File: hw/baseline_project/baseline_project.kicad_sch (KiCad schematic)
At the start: 17 parts, among them J101 EXT_3V3, Q101 IRLD024PBF, SW101 UP, SW102 DOWN, SW103 LEFT, SW104 RIGHT, SW105 MODE, U101 EK-TM4C123GXL, U102 ESP8266-01/ESP-01, U103 Adafruit ST7735R

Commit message: schematic
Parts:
- removed D101: 1V0, Diode_THT:D_5W_P12.70mm_Horizontal, symbol Device:D_Small
- removed LS101: Speaker, Connector_PinHeader_2.54mm:PinHeader_1x02_P2.54mm_Vertical, symbol Device:Speaker
- removed Q101: IRLD024PBF, footprints:vishay_IRLD024PBF, symbol Simulation_SPICE:NMOS
- added C1: 1uF, symbol Device:C
- added C2: 0.1uF, symbol Device:C
- added C3, C4, C5: 4.7uF, symbol Device:C
- added IC1: LM4041CILPR, ECE445L:ti_LM4041CILPR, symbol ti_LM4041CILPR:LM4041CILPR
- added J1: AudioJack, ECE445L:Jack_3.5mm_CUI_SJ1-3523N_Horizontal, symbol ECE445L:HeadphoneJack
- added JP1: Jumper_3_Open, ECE445L:PinHeader_1x03_P2.54mm_Vertical, symbol ECE445L:Jumper_3_Open
- added R1: 20k, symbol Device:R
- added R10, R2, R5, R6, R7, R8, R9: 10k, symbol Device:R
- added R11: 10k, ECE445L:Potentiometer, symbol ECE445L:Potentiometer
- added R3: 2k, symbol Device:R
- added R4: 47k, symbol Device:R
- added TP1, TP2, TP3, TP4, TP5, TP6: TP, ECE445L:Testpoint_1x02_P2.54mm, symbol ECE445L:Testpoint
- added U1: TLV5616CP, symbol ti_TLV5616CP:TLV5616CP
- added U2: MCP34119P, Package_DIP:DIP-8_W7.62mm_LongPads, symbol motorola_MCP34119P:MCP34119P
- added U3: LM2937xMP, Package_TO_SOT_SMD:SOT-223-3_TabPin2, symbol Regulator_Linear:LM2937xMP
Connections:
- net +3V3: now also SW101.1, SW102.1, SW103.1, SW104.1, SW105.1, JP1.1 (A), R11.1, TP5.1 (A), TP5.2 (B)
- net +5V: now also C4.1, TP4.1 (A), TP4.2 (B), U3.1 (VI)
- net GND: now also C1.2, C3.2, C4.2, C5.2, IC1.3, R10.2, R11.3, R5.2, R6.2, R7.2, R8.2, R9.2, TP6.1 (A), TP6.2 (B), U1.3 (*CS), U1.5 (AGND), U2.1 (CD), U2.7 (GND), U3.2 (GND); no longer SW101.1, SW102.1, SW103.1, SW104.1, SW105.1
- net SW_DOWN: now also R7.1
- net SW_LEFT: now also R8.1
- net SW_MODE: now also R10.1
- net SW_RIGHT: now also R9.1
- net SW_UP: now also R6.1
- net WIFI_3V3: now also C5.1, U3.3 (VO)
- net SS1_SCLK: now reaches U101.J3_3 (PD0)
- net SS1_SCLK: now also U1.2 (SCLK)
- net SS1_FS: now reaches U101.J3_4 (PD1)
- net SS1_FS: now also U1.4 (FS)
- net SSI1_TX: now reaches U101.J3_6 (PD3)
- net SSI1_TX: now also U1.1 (DIN)
- net SPEAKER_GATE: no longer names the net of U101.J1_4 (PB1)
- new net: C3.1, U2.2 (FC2)
- new net: C1.1, U2.3 (FC1)
- new net: R1.2, R2.1, U2.4 (VIN)
- new net: J1.R (ring), J1.T (tip), R2.2, TP3.1 (A), U2.5 (VO1)
- new net: J1.S (sleeve), TP3.2 (B), U2.8 (VO2)
- new net: C2.2, TP2.1 (A), TP2.2 (B), U1.7 (OUT)
- new net: IC1.1, R4.2, R5.1
- new net: C2.1, R1.1
- new net DAC_Amp_Ctrl: JP1.2 (C), R3.1, TP1.1 (A), TP1.2 (B), U1.8 (VDD)
- new net Pot_Out: JP1.3 (B), R11.2
- new net VREF: IC1.2, R3.2, R4.1, U1.6 (REFIN)
- no-connect marks 19 -> 17
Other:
- note removed: "SS1_FS"
- note removed: "SS1_MOSI"
- note removed: "SS1_SCK"

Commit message: slight edit schematic
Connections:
- net +3V3: no longer R11.1
- net DAC_Amp_Ctrl: no longer U1.8 (VDD)
- net Pot_Out: no longer R11.2
- net at J1.S (sleeve), U2.8 (VO2): no longer TP3.2 (B)
- new net: R11.1, R2.2, U2.5 (VO1)
- new net: J1.R (ring), J1.T (tip), R11.2
- now unconnected: TP3.1 (A)
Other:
- moved on the sheet: R11
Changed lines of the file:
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@@
   (junction (at 78.232 152.146) (diameter 0) (color 0 0 0 0)
   )
-  (junction (at 132.334 158.75) (diameter 0) (color 0 0 0 0)
-  )
   (junction (at 159.512 116.078) (diameter 0) (color 0 0 0 0)
   )
@@
   (junction (at 135.89 45.72) (diameter 0) (color 0 0 0 0)
   )
-  (junction (at 134.112 161.29) (diameter 0) (color 0 0 0 0)
-  )
   (junction (at 97.282 169.926) (diameter 0) (color 0 0 0 0)
   )
   (junction (at 51.308 120.904) (diameter 0) (color 0 0 0 0)
   )
-  (junction (at 130.302 155.956) (diameter 0) (color 0 0 0 0)
-  )
   (junction (at 99.06 102.87) (diameter 0) (color 0 0 0 0)
   )
   (junction (at 60.96 90.17) (diameter 0) (color 0 0 0 0)
   )
+  (junction (at 134.874 166.624) (diameter 0) (color 0 0 0 0)
+  )
+  (junction (at 125.476 155.956) (diameter 0) (color 0 0 0 0)
+  )
   (junction (at 143.51 62.23) (diameter 0) (color 0 0 0 0)
   )
@@
   )
   (junction (at 82.042 152.146) (diameter 0) (color 0 0 0 0)
-  )
-  (junction (at 125.476 155.956) (diameter 0) (color 0 0 0 0)
   )
   (no_connect (at 60.96 49.53))
@@
     (stroke (width 0) (type default))
   )
-  (wire (pts (xy 132.334 166.624) (xy 135.382 166.624))
+  (wire (pts (xy 132.334 166.624) (xy 134.874 166.624))
+    (stroke (width 0) (type default))
+  )
+  (wire (pts (xy 131.064 184.912) (xy 131.191 184.912))
     (stroke (width 0) (type default))
   )
@@
     (stroke (width 0) (type default))
   )
+  (wire (pts (xy 125.476 155.956) (xy 131.064 155.956))
+    (stroke (width 0) (type default))
+  )
   (wire (pts (xy 94.488 152.146) (xy 97.79 152.146))
     (stroke (width 0) (type default))
@@
     (stroke (width 0) (type default))
   )
-  (wire (pts (xy 132.334 155.956) (xy 132.334 158.75))
-    (stroke (width 0) (type default))
-  )
   (wire (pts (xy 194.056 58.674) (xy 194.056 61.214))
     (stroke (width 0) (type default))
   )
+  (wire (pts (xy 131.064 183.388) (xy 131.064 184.912))
+    (stroke (width 0) (type default))
+  )
   (wire (pts (xy 88.9 124.46) (xy 99.06 124.46))
     (stroke (width 0) (type default))
@@
     (stroke (width 0) (type default))
   )
-  (wire (pts (xy 33.782 126.746) (xy 38.354 126.746))
-    (stroke (width 0) (type default))
-  )
   (wire (pts (xy 140.97 45.72) (xy 147.32 45.72))
     (stroke (width 0) (type default))
@@
     (stroke (width 0) (type default))
   )
-  (wire (pts (xy 134.112 149.606) (xy 134.112 161.29))
-    (stroke (width 0) (type default))
-  )
   (wire (pts (xy 132.334 158.75) (xy 132.334 166.624))
     (stroke (width 0) (type default))
@@
     (stroke (width 0) (type default))
   )
+  (wire (pts (xy 131.064 155.956) (xy 131.064 175.768))
+    (stroke (width 0) (type default))
+  )
   (wire (pts (xy 131.826 110.49) (xy 131.826 114.3))
     (stroke (width 0) (type default))
@@
     (stroke (width 0) (type default))
   )
-  (wire (pts (xy 134.112 161.29) (xy 135.382 161.29))
+  (wire (pts (xy 129.032 161.29) (xy 135.382 161.29))
     (stroke (width 0) (type default))
   )
@@
     (stroke (width 0) (type default))
   )
-  (wire (pts (xy 130.302 155.956) (xy 132.334 155.956))
-    (stroke (width 0) (type default))
-  )
   (wire (pts (xy 37.592 162.306) (xy 34.544 162.306))
     (stroke (width 0) (type default))
@@
     (stroke (width 0) (type default))
   )
+  (wire (pts (xy 134.874 166.624) (xy 134.874 179.578))
+    (stroke (width 0) (type default))
+  )
   (wire (pts (xy 205.994 58.166) (xy 206.248 58.166))
     (stroke (width 0) (type default))
@@
     (stroke (width 0) (type default))
   )
-  (wire (pts (xy 129.032 161.29) (xy 134.112 161.29))
-    (stroke (width 0) (type default))
-  )
   (wire (pts (xy 154.94 156.21) (xy 159.766 156.21))
     (stroke (width 0) (type default))
   )
-  (wire (pts (xy 130.302 149.606) (xy 130.302 155.956))
-    (stroke (width 0) (type default))
-  )
   (wire (pts (xy 135.89 30.48) (xy 147.32 30.48))
     (stroke (width 0) (type default))
@@
     (stroke (width 0) (type default))
   )
+  (wire (pts (xy 134.874 166.624) (xy 135.382 166.624))
+    (stroke (width 0) (type default))
+  )
   (wire (pts (xy 132.334 158.75) (xy 135.382 158.75))
     (stroke (width 0) (type default))
@@
   )
   (wire (pts (xy 130.81 62.23) (xy 143.51 62.23))
-    (stroke (width 0) (type default))
-  )
-  (wire (pts (xy 125.476 155.956) (xy 130.302 155.956))
     (stroke (width 0) (type default))
   )
@@
     (effects (font (size 1.27 1.27) bold) (justify right bottom))
   )
-  (label "DAC_Amp_Ctrl" (at 39.624 172.466 0) (fields_autoplaced)
-    (effects (font (size 1.27 1.27)) (justify left bottom))
-  )
   (label "SW_MODE" (at 60.96 85.09 0) (fields_autoplaced)
     (effects (font (size 1.27 1.27) bold) (justify left bottom))
@@
   (label "TFT_MOSI" (at 25.4 46.99 180) (fields_autoplaced)
     (effects (font (size 1.27 1.27) bold) (justify right bottom))
-  )
-  (label "Pot_Out" (at 38.354 126.746 0) (fields_autoplaced)
-    (effects (font (size 1.27 1.27)) (justify left bottom))
   )
   (label "SW_DOWN" (at 99.06 114.3 0) (fields_autoplaced)
@@
     )
   )
-  (symbol (lib_id "power:GND") (at 29.972 130.556 0) (unit 1)
-    (in_bom yes) (on_board yes) (dnp no) (fields_autoplaced)
-    (property "Reference" "#PWR08" (at 29.972 136.906 0)
-      (effects (font (size 1.27 1.27)) hide)
-    )
-    (property "Value" "GND" (at 29.972 135.128 0)
-      (effects (font (size 1.27 1.27)))
-    )
-    (property "Footprint" "" (at 29.972 130.556 0)
-      (effects (font (size 1.27 1.27)) hide)
-    )
-    (property "Datasheet" "" (at 29.972 130.556 0)
+  (symbol (lib_id "power:GND") (at 131.191 184.912 0) (unit 1)
+    (in_bom yes) (on_board yes) (dnp no) (fields_autoplaced)
+    (property "Reference" "#PWR08" (at 131.191 191.262 0)
+      (effects (font (size 1.27 1.27)) hide)
+    )
+    (property "Value" "GND" (at 131.191 189.484 0)
+      (effects (font (size 1.27 1.27)))
+    )
+    (property "Footprint" "" (at 131.191 184.912 0)
+      (effects (font (size 1.27 1.27)) hide)
+    )
+    (property "Datasheet" "" (at 131.191 184.912 0)
       (effects (font (size 1.27 1.27)) hide)
     )
@@
     )
   )
-  (symbol (lib_id "ECE445L:Potentiometer") (at 28.067 126.746 0) (unit 1)
-    (in_bom yes) (on_board yes) (dnp no) (fields_autoplaced)
-    (property "Reference" "R11" (at 27.813 125.476 0)
+  (symbol (lib_id "ECE445L:Potentiometer") (at 129.159 179.578 0) (unit 1)
+    (in_bom yes) (on_board yes) (dnp no) (fields_autoplaced)
+    (property "Reference" "R11" (at 128.905 178.308 0)
       (effects (font (size 1.27 1.27)) (justify right))
     )
-    (property "Value" "10k" (at 27.813 128.016 0)
+    (property "Value" "10k" (at 128.905 180.848 0)
       (effects (font (size 1.27 1.27)) (justify right))
     )
-    (property "Footprint" "ECE445L:Potentiometer" (at 28.067 126.746 0)
-      (effects (font (size 1.27 1.27)) hide)
-    )
-    (property "Datasheet" "" (at 28.067 126.746 0)
+    (property "Footprint" "ECE445L:Potentiometer" (at 129.159 179.578 0)
+      (effects (font (size 1.27 1.27)) hide)
+    )
+    (property "Datasheet" "" (at 129.159 179.578 0)
       (effects (font (size 1.27 1.27)) hide)
     )
@@
         )
       )
-    )
-  )
-  (symbol (lib_id "power:+3V3") (at 29.972 122.936 0) (unit 1)
-    (in_bom yes) (on_board yes) (dnp no)
-    (property "Reference" "#PWR09" (at 29.972 126.746 0)
-      (effects (font (size 1.27 1.27)) hide)
-    )
-    (property "Value" "+3V3" (at 26.162 121.666 0)
-      (effects (font (size 1.27 1.27)))
-    )
-    (property "Footprint" "" (at 29.972 122.936 0)
-      (effects (font (size 1.27 1.27)) hide)
-    )
-    (property "Datasheet" "" (at 29.972 122.936 0)
-      (effects (font (size 1.27 1.27)) hide)
-    )
-    (pin "1")
-    (instances
-      (project "baseline_project"
-        (path "/69b823fd-c065-40ff-9bb9-c5835555f3eb"
-          (reference "#PWR09") (unit 1)
-        )
-      )

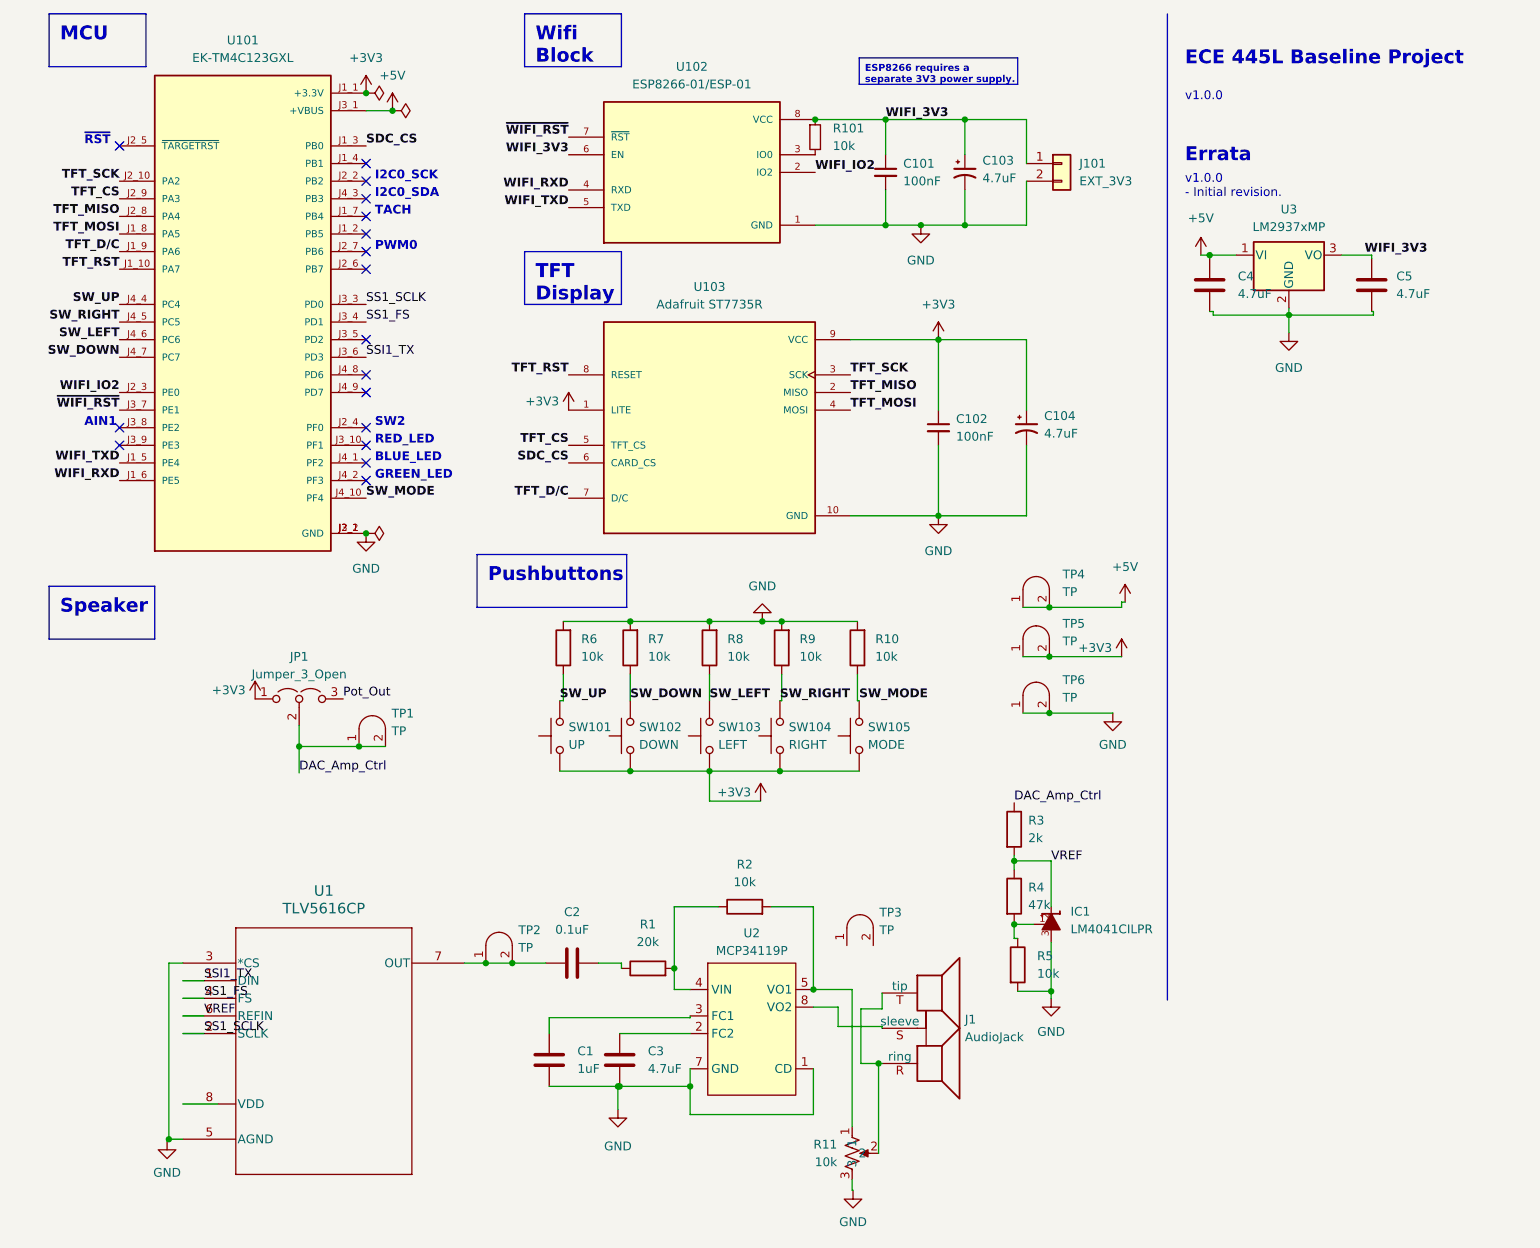
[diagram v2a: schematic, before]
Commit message: schematic done, pcb design
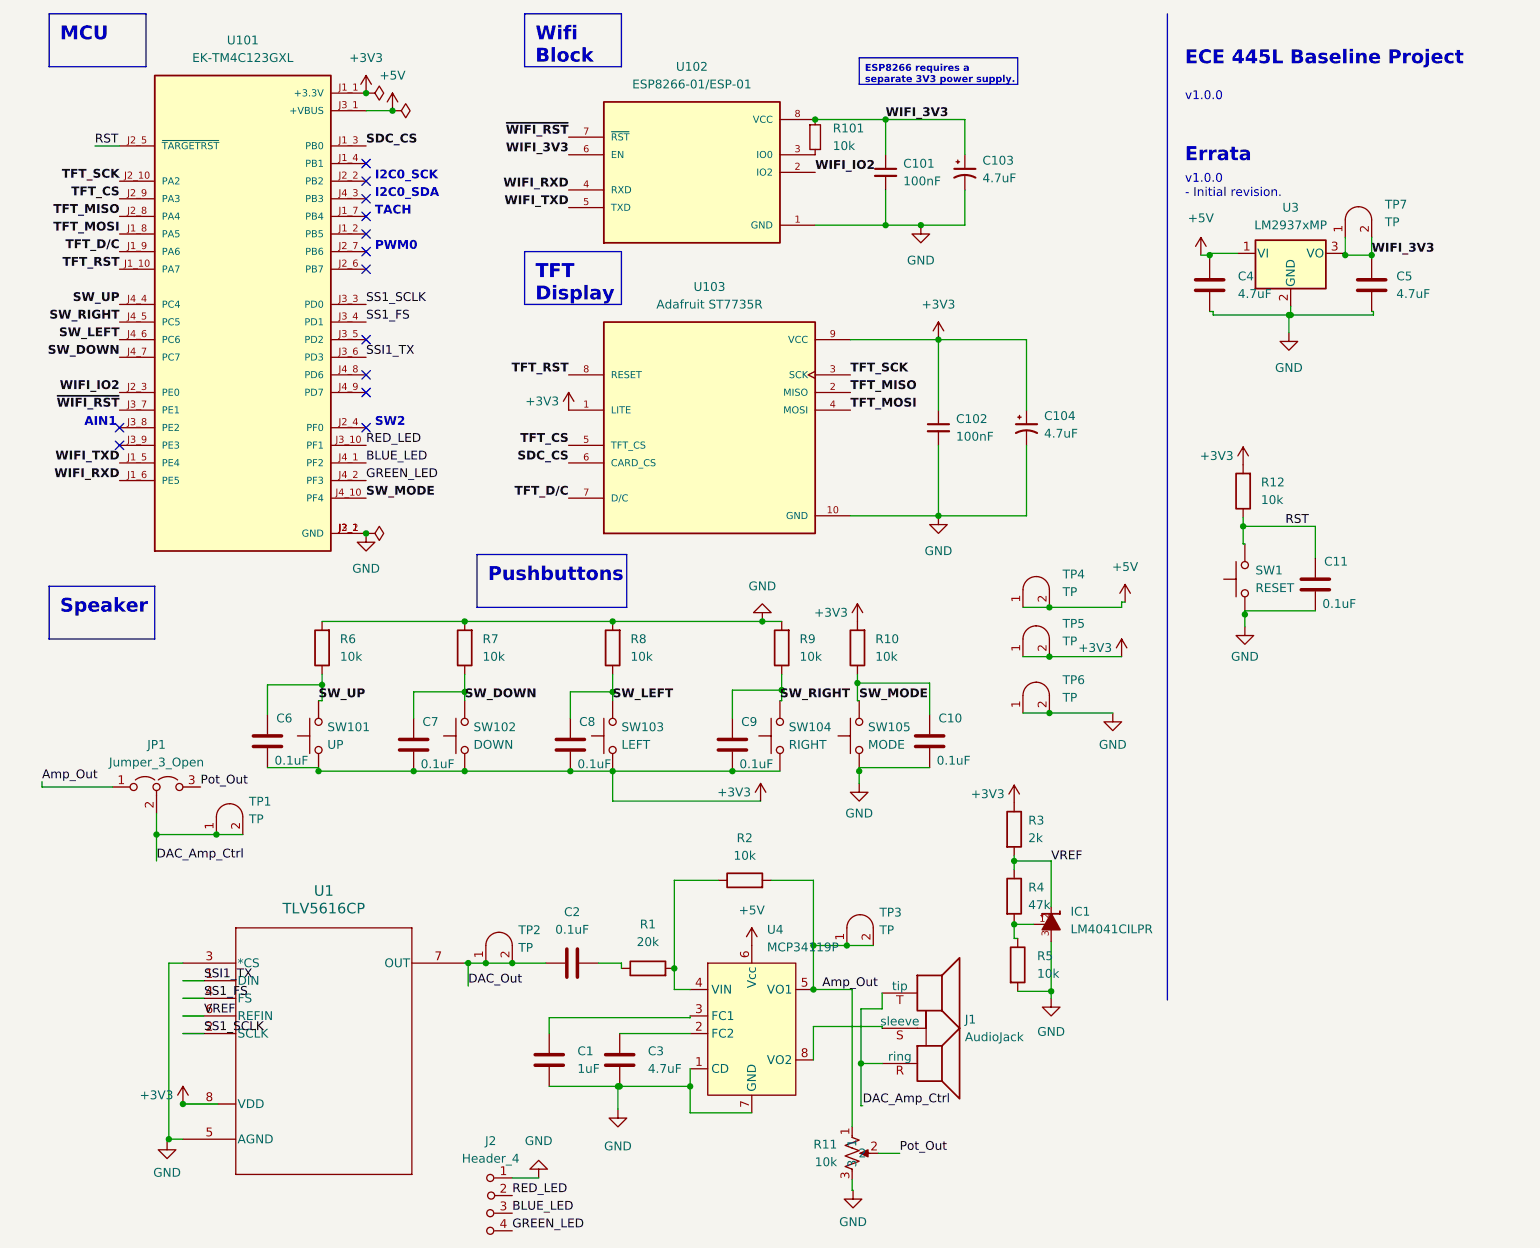
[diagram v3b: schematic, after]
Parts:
- removed J101: EXT_3V3, Connector_Samtec_HPM_THT:Samtec_HPM-02-01-x-S_Straight_1x02_Pitch5.08mm, symbol Connector_Generic:Conn_01x02
- removed U2: MCP34119P, Package_DIP:DIP-8_W7.62mm_LongPads, symbol motorola_MCP34119P:MCP34119P
- added C10, C11, C6, C7, C8, C9: 0.1uF, ECE445L:C_Axial_200mil, symbol ECE445L:C
- added J2: Header_4, ECE445L:PinHeader_1x04_P2.54mm_Vertical, symbol ECE445L:Header_4
- added R12: 10k, Resistor_THT:R_Axial_DIN0207_L6.3mm_D2.5mm_P10.16mm_Horizontal, symbol Device:R
- added SW1: RESET, Button_Switch_THT:SW_PUSH_6mm, symbol Switch:SW_Push
- added TP7: TP, ECE445L:Testpoint_1x02_P2.54mm, symbol ECE445L:Testpoint
- added U4: MCP34119P, ECE445L:DIP-8_W7.62mm_LongPads, symbol ECE445L:MCP34119P
- C1, C2, C3, C4, C5: footprint (none) -> ECE445L:C_Axial_200mil
- C101, C102: footprint Capacitor_THT:C_Axial_L5.1mm_D3.1mm_P15.00mm_Horizontal -> ECE445L:C_Axial_200mil
- C103, C104: footprint Capacitor_THT:CP_Axial_L10.0mm_D4.5mm_P15.00mm_Horizontal -> ECE445L:CP_Radial_Tantal200mil
- R1, R10, R2, R3, R4, R5, R6, R7, R8, R9: footprint (none) -> Resistor_THT:R_Axial_DIN0207_L6.3mm_D2.5mm_P10.16mm_Horizontal
- R101: footprint Resistor_THT:R_Axial_DIN0411_L9.9mm_D3.6mm_P15.24mm_Horizontal -> Resistor_THT:R_Axial_DIN0207_L6.3mm_D2.5mm_P10.16mm_Horizontal
- U1: footprint (none) -> ECE445L:ul_TLV5616CP
- U101: footprint footprints:ti_EKTM4C123GXL -> ECE445L:ti_EKTM4C123GXL
- U102: footprint footprints:ai_thinker_ESP8266_01 -> ECE445L:ai_thinker_ESP8266_01
- U103: footprint footprints:adafruit_st7735r -> ECE445L:adafruit_st7735r
- U3: footprint Package_TO_SOT_SMD:SOT-223-3_TabPin2 -> ECE445L:LM2937
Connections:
- net +3V3: now also R10.2, R3.1, U1.8 (VDD), C6.2, C7.2, C8.2, C9.2, R12.2; no longer JP1.1 (A), SW105.1
- net +5V: now also U4.6 (Vcc)
- net DAC_Amp_Ctrl: now also J1.R (ring), J1.T (tip); no longer R3.1
- net GND: now also SW105.1, C10.2, C11.2, J2.1 (A), SW1.1, U4.1 (CD), U4.7 (GND); no longer R10.2
- net Pot_Out: now also R11.2
- net SW_DOWN: now also C7.1
- net SW_LEFT: now also C8.1
- net SW_MODE: now also C10.1
- net SW_RIGHT: now also C9.1
- net SW_UP: now also C6.1
- net WIFI_3V3: now also TP7.1 (A), TP7.2 (B)
- net at C3.1: now also U4.2 (FC2)
- net at C1.1: now also U4.3 (FC1)
- net at R1.2, R2.1: now also U4.4 (VIN)
- net Amp_Out: now reaches R11.1, R2.2
- net Amp_Out: now also JP1.1 (A), TP3.1 (A), TP3.2 (B), U4.5 (VO1)
- net at J1.S (sleeve): now also U4.8 (VO2)
- net DAC_Out: now reaches C2.2, TP2.1 (A), TP2.2 (B), U1.7 (OUT)
- net RST: now reaches U101.J2_5 (~{TARGETRST})
- net RST: now also C11.1, R12.1, SW1.2
- net RED_LED: now reaches U101.J3_10 (PF1)
- net RED_LED: now also J2.2 (B)
- net BLUE_LED: now reaches U101.J4_1 (PF2)
- net BLUE_LED: now also J2.3 (C)
- net GREEN_LED: now reaches U101.J4_2 (PF3)
- net GREEN_LED: now also J2.4 (C)
- no-connect marks 17 -> 13
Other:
- note removed: "BLUE_LED"
- note removed: "GREEN_LED"
- note removed: "RED_LED"
- note removed: "~{RST}"
- moved on the sheet: JP1, R2, R6, R7, R8, SW101, SW102, SW103, TP1

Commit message: placement ST7735 board
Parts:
- removed R10, R6, R7, R8, R9: 10k, Resistor_THT:R_Axial_DIN0207_L6.3mm_D2.5mm_P10.16mm_Horizontal, symbol Device:R
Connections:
- net +3V3: no longer C6.2, C7.2, C8.2, C9.2, SW101.1, SW102.1, SW103.1, SW104.1
- net GND: now also C6.2, C7.2, C8.2, C9.2, J1.S (sleeve), SW101.1, SW102.1, SW103.1, SW104.1
- net at U4.8 (VO2): no longer J1.S (sleeve)
- no-connect marks 13 -> 14
